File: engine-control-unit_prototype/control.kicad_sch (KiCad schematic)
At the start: 24 parts, among them J18 VALVE_IPA, J19 VALVE_NOS, J20 HEATER_IPA, J21 HEATER_NOS, Q2 NMOS, Q3 NPN, Q4 NMOS, Q5 NPN, Q6 NPN

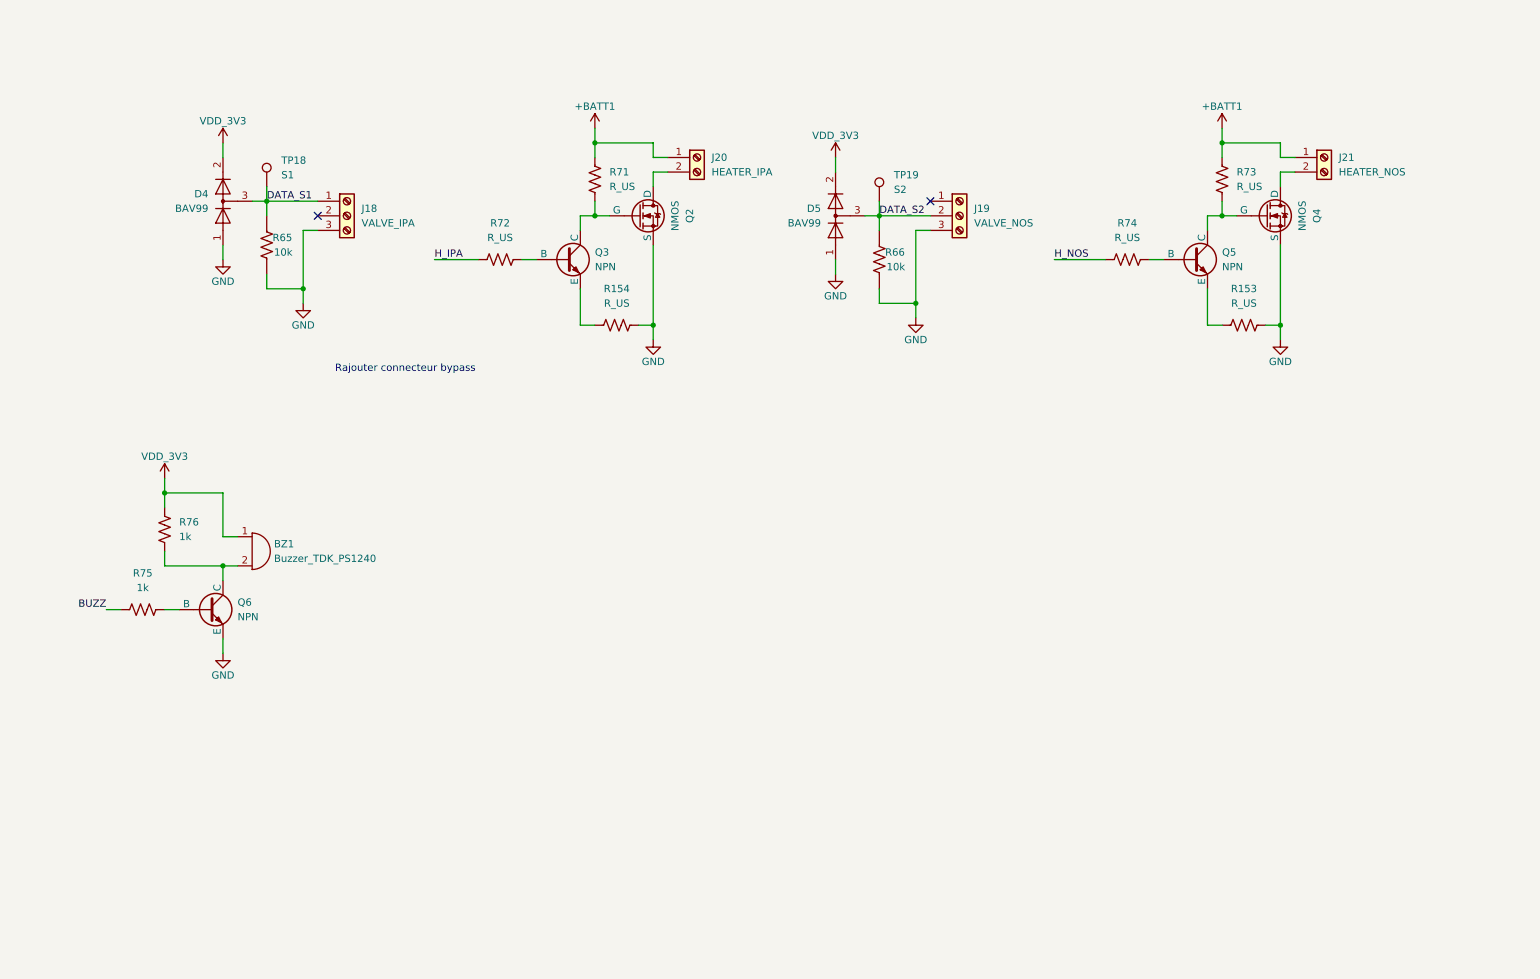
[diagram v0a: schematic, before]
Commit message: Added magnetic encoders Added optional external valve control connector
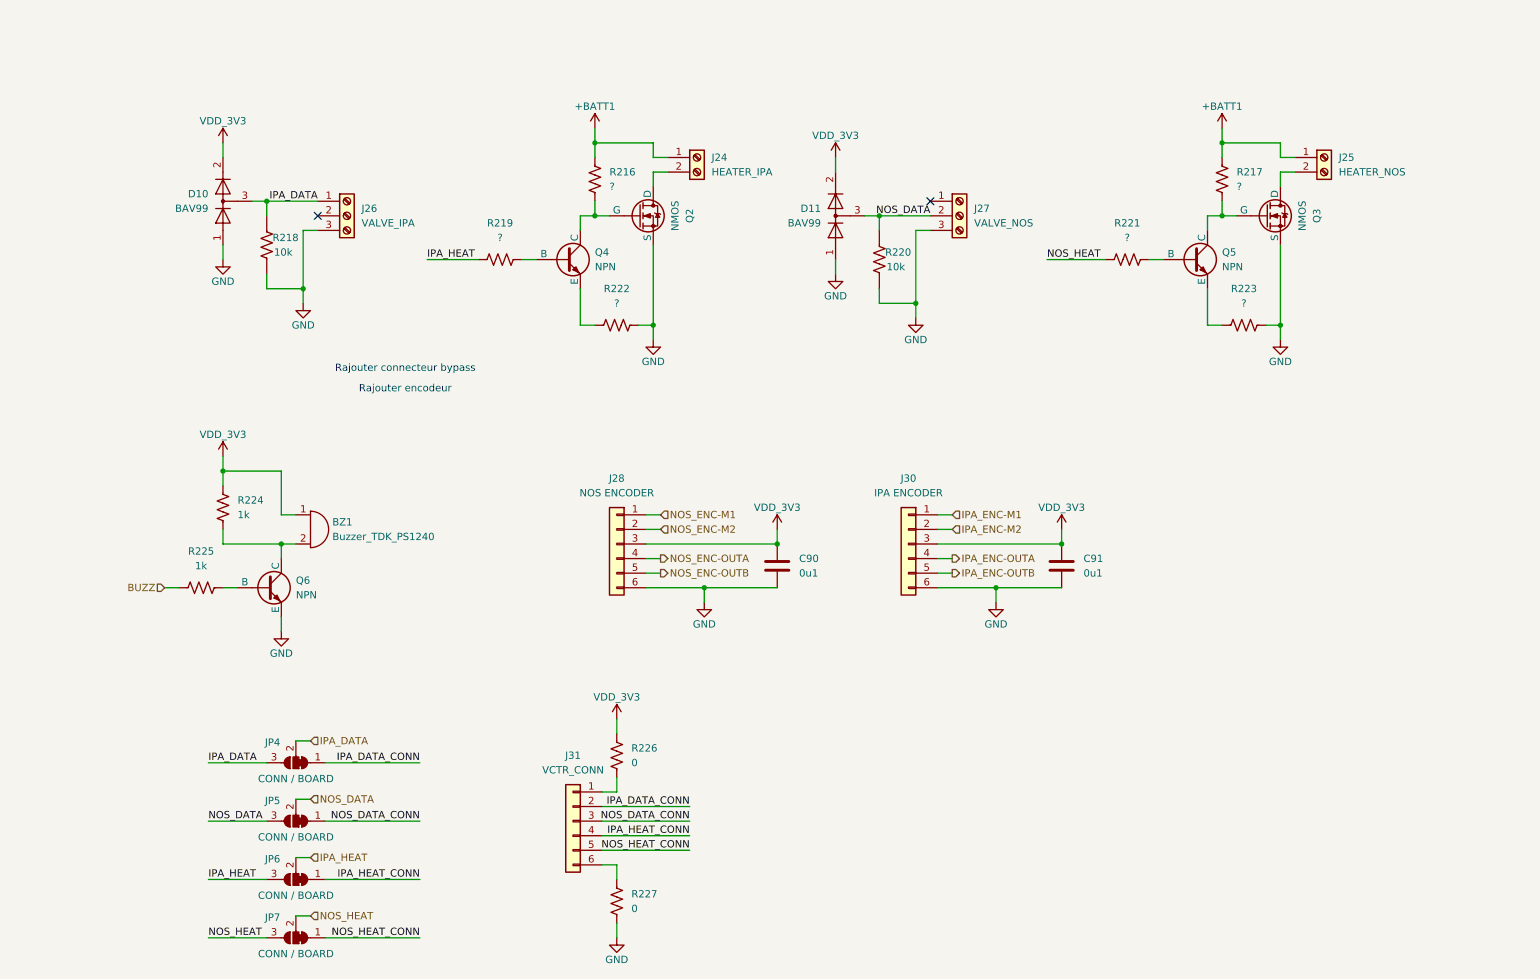
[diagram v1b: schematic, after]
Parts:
- removed TP18: S1, symbol Connector:TestPoint
- removed TP19: S2, symbol Connector:TestPoint
- added C90, C91: 0u1, symbol Device:C
- added J28: NOS ENCODER, symbol Connector_Generic:Conn_01x06
- added J30: IPA ENCODER, symbol Connector_Generic:Conn_01x06
- added J31: VCTR_CONN, symbol Connector_Generic:Conn_01x06
- added JP4, JP5, JP6, JP7: CONN / BOARD, symbol Jumper:SolderJumper_3_Bridged12
- added R226, R227: 0, symbol Device:R_US
- R216: renamed from R71; value R_US -> ?
- R217: renamed from R73; value R_US -> ?
- R219: renamed from R72; value R_US -> ?
- R221: renamed from R74; value R_US -> ?
- R222: renamed from R154; value R_US -> ?
- R223: renamed from R153; value R_US -> ?
- renumbered D4 to D10, D5 to D11, J20 to J24, J21 to J25, J18 to J26, J19 to J27, Q4 to Q3, Q3 to Q4, R65 to R218, R66 to R220, R76 to R224, R75 to R225
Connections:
- net GND: now also C90.2, C91.2, J28.6 (Pin_6), J30.6 (Pin_6), R227.2
- net VDD_3V3: now also C90.1, C91.1, J28.3 (Pin_3), J30.3 (Pin_3), R226.1
- net DATA_S1 renamed IPA_DATA
- net IPA_DATA: now also JP4.2 (C), JP4.3 (B)
- net DATA_S2 renamed NOS_DATA
- net NOS_DATA: now also JP5.2 (C), JP5.3 (B)
- net H_IPA renamed IPA_HEAT
- net IPA_HEAT: now also JP6.2 (C), JP6.3 (B)
- net H_NOS renamed NOS_HEAT
- net NOS_HEAT: now also JP7.2 (C), JP7.3 (B)
- new net: J31.1 (Pin_1), R226.2
- new net: J31.6 (Pin_6), R227.1
- new net IPA_DATA_CONN: J31.2 (Pin_2), JP4.1 (A)
- new net IPA_ENC-M1: J30.1 (Pin_1)
- new net IPA_ENC-M2: J30.2 (Pin_2)
- new net IPA_ENC-OUTA: J30.4 (Pin_4)
- new net IPA_ENC-OUTB: J30.5 (Pin_5)
- new net IPA_HEAT_CONN: J31.4 (Pin_4), JP6.1 (A)
- new net NOS_DATA_CONN: J31.3 (Pin_3), JP5.1 (A)
- new net NOS_ENC-M1: J28.1 (Pin_1)
- new net NOS_ENC-M2: J28.2 (Pin_2)
- new net NOS_ENC-OUTA: J28.4 (Pin_4)
- new net NOS_ENC-OUTB: J28.5 (Pin_5)
- new net NOS_HEAT_CONN: J31.5 (Pin_5), JP7.1 (A)
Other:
- note added: "Rajouter encodeur"
- moved on the sheet: BZ1, Q6, R224, R225

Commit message: VDD_3V3 is now VDD_3V6 (Removed LDO) LEDs now have the right symbol (oops x2)
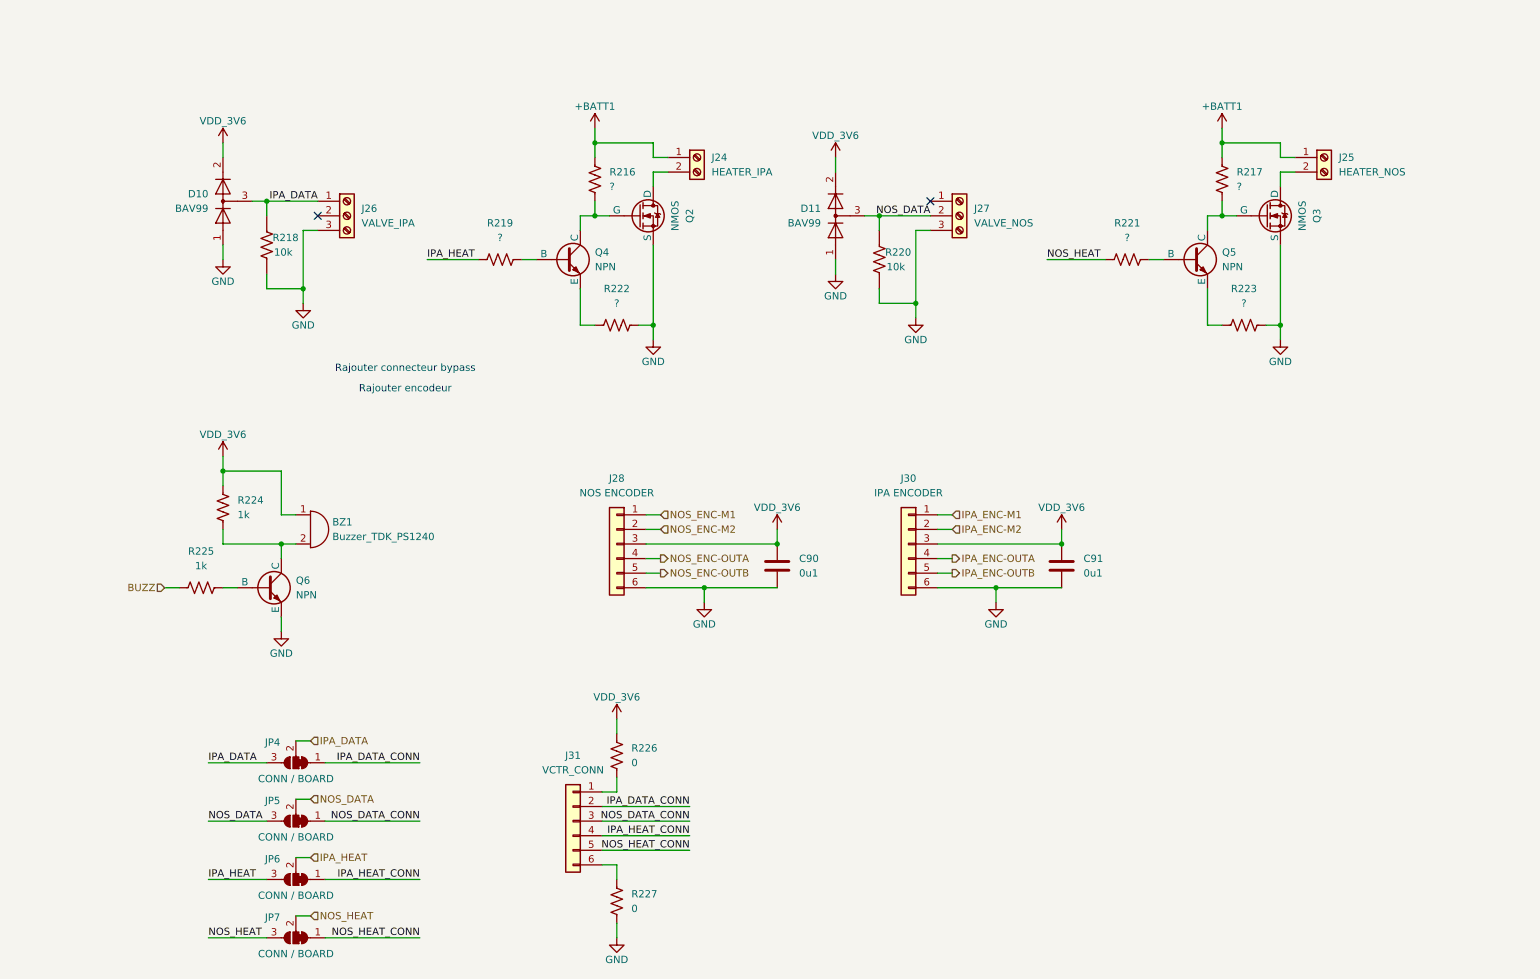
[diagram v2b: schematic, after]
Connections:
- net VDD_3V3 renamed VDD_3V6
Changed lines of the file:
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@@
 			)
 		)
-		(property "Value" "VDD_3V3"
+		(property "Value" "VDD_3V6"
 			(at 149.86 100.33 0)
 			(effects
@@
 		(on_board yes)
 		(dnp no)
-		(property "Reference" "#PWR?"
+		(property "Reference" "#PWR0145"
 			(at 53.34 95.25 0)
 			(effects
@@
 			)
 		)
-		(property "Value" "VDD_3V3"
+		(property "Value" "VDD_3V6"
 			(at 53.34 87.63 0)
 			(effects
@@
 			(project "engine-control-unit_prototype"
 				(path "/4da294f1-7505-49eb-91fe-5b5cfad6e8fb/b1c03273-6499-41ff-b1a3-3c63c73b0d1a"
-					(reference "#PWR?")
+					(reference "#PWR0145")
 					(unit 1)
 				)
@@
 		(on_board yes)
 		(dnp no)
-		(property "Reference" "#PWR?"
+		(property "Reference" "#PWR0152"
 			(at 67.31 71.12 0)
 			(effects
@@
 			(project "engine-control-unit_prototype"
 				(path "/4da294f1-7505-49eb-91fe-5b5cfad6e8fb/b1c03273-6499-41ff-b1a3-3c63c73b0d1a"
-					(reference "#PWR?")
+					(reference "#PWR0152")
 					(unit 1)
 				)
@@
 		(on_board yes)
 		(dnp no)
-		(property "Reference" "#PWR?"
+		(property "Reference" "#PWR0150"
 			(at 160.02 66.04 0)
 			(effects
@@
 			(project "engine-control-unit_prototype"
 				(path "/4da294f1-7505-49eb-91fe-5b5cfad6e8fb/b1c03273-6499-41ff-b1a3-3c63c73b0d1a"
-					(reference "#PWR?")
+					(reference "#PWR0150")
 					(unit 1)
 				)
@@
 		(on_board yes)
 		(dnp no)
-		(property "Reference" "#PWR?"
+		(property "Reference" "#PWR0147"
 			(at 128.27 77.47 0)
 			(effects
@@
 			(project "engine-control-unit_prototype"
 				(path "/4da294f1-7505-49eb-91fe-5b5cfad6e8fb/b1c03273-6499-41ff-b1a3-3c63c73b0d1a"
-					(reference "#PWR?")
+					(reference "#PWR0147")
 					(unit 1)
 				)
@@
 			)
 		)
-		(property "Value" "VDD_3V3"
+		(property "Value" "VDD_3V6"
 			(at 121.92 133.35 0)
 			(effects
@@
 			)
 		)
-		(property "Value" "VDD_3V3"
+		(property "Value" "VDD_3V6"
 			(at 199.39 100.33 0)
 			(effects
@@
 		(on_board yes)
 		(dnp no)
-		(property "Reference" "#PWR?"
+		(property "Reference" "#PWR0149"
 			(at 173.99 73.66 0)
 			(effects
@@
 			(project "engine-control-unit_prototype"
 				(path "/4da294f1-7505-49eb-91fe-5b5cfad6e8fb/b1c03273-6499-41ff-b1a3-3c63c73b0d1a"
-					(reference "#PWR?")
+					(reference "#PWR0149")
 					(unit 1)
 				)
@@
 		(on_board yes)
 		(dnp no)
-		(property "Reference" "#PWR?"
+		(property "Reference" "#PWR0154"
 			(at 53.34 40.64 0)
 			(effects
@@
 			)
 		)
-		(property "Value" "VDD_3V3"
+		(property "Value" "VDD_3V6"
 			(at 53.34 33.02 0)
 			(effects
@@
 			(project "engine-control-unit_prototype"
 				(path "/4da294f1-7505-49eb-91fe-5b5cfad6e8fb/b1c03273-6499-41ff-b1a3-3c63c73b0d1a"
-					(reference "#PWR?")
+					(reference "#PWR0154")
 					(unit 1)
 				)
@@
 		(on_board yes)
 		(dnp no)
-		(property "Reference" "#PWR?"
+		(property "Reference" "#PWR0153"
 			(at 53.34 63.5 0)
 			(effects
@@
 			(project "engine-control-unit_prototype"
 				(path "/4da294f1-7505-49eb-91fe-5b5cfad6e8fb/b1c03273-6499-41ff-b1a3-3c63c73b0d1a"
-					(reference "#PWR?")
+					(reference "#PWR0153")
 					(unit 1)
 				)
@@
 		(on_board yes)
 		(dnp no)
-		(property "Reference" "#PWR?"
+		(property "Reference" "#PWR0148"
 			(at 160.02 43.18 0)
 			(effects
@@
 			)
 		)
-		(property "Value" "VDD_3V3"
+		(property "Value" "VDD_3V6"
 			(at 160.02 35.56 0)
 			(effects
@@
 			(project "engine-control-unit_prototype"
 				(path "/4da294f1-7505-49eb-91fe-5b5cfad6e8fb/b1c03273-6499-41ff-b1a3-3c63c73b0d1a"
-					(reference "#PWR?")
+					(reference "#PWR0148")
 					(unit 1)
 				)
@@
 		(on_board yes)
 		(dnp no)
-		(property "Reference" "#PWR?"
+		(property "Reference" "#PWR0151"
 			(at 237.49 77.47 0)
 			(effects
@@
 			(project "engine-control-unit_prototype"
 				(path "/4da294f1-7505-49eb-91fe-5b5cfad6e8fb/b1c03273-6499-41ff-b1a3-3c63c73b0d1a"
-					(reference "#PWR?")
+					(reference "#PWR0151")
 					(unit 1)
 				)
@@
 		(on_board yes)
 		(dnp no)
-		(property "Reference" "#PWR?"
+		(property "Reference" "#PWR0146"
 			(at 63.5 128.27 0)
 			(effects
@@
 			(project "engine-control-unit_prototype"
 				(path "/4da294f1-7505-49eb-91fe-5b5cfad6e8fb/b1c03273-6499-41ff-b1a3-3c63c73b0d1a"
-					(reference "#PWR?")
+					(reference "#PWR0146")
 					(unit 1)
 				)

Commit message: Started layout Added some footprints
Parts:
- C90, C91: footprint (none) -> Capacitor_SMD:C_0402_1005Metric
- D10, D11, Q2, Q3, Q4, Q5, R216, R217, R218, R219, R220, R221, R222, R223: now not fitted
- J24, J25: footprint (none) -> Connector_PinSocket_2.54mm:PinSocket_1x02_P2.54mm_Vertical
- J26, J27: footprint (none) -> Connector_PinSocket_2.54mm:PinSocket_1x03_P2.54mm_Vertical
- J28, J30, J31: footprint (none) -> Connector_PinSocket_2.54mm:PinSocket_1x06_P2.54mm_Vertical
- JP4, JP5, JP6, JP7: footprint (none) -> Jumper:SolderJumper-3_P1.3mm_Bridged12_RoundedPad1.0x1.5mm
- R226, R227: footprint (none) -> Resistor_SMD:R_0201_0603Metric
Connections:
- net VDD_3V6 renamed VDD_3V3
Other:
- note added: "DNF"
- moved on the sheet: J24, J25, J26, J27
